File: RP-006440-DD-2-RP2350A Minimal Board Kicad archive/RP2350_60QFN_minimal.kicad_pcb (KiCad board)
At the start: 2 copper layers, 52 x 51 mm, 45 parts, among them J1 USB_C_Receptacle_USB2.0_16P, J2 Conn_02x18_Odd_Even, J3 Conn_02x18_Odd_Even, J4 SM03B-SRSS-TB, SW1 SW_Push, SW2 SW_Push, U1 RP2350_60QFN, U2 NCP1117-3.3_SOT223, U3 W25Q128JVS, Y1 ABM8-272-T3

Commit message: Schematic text
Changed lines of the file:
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@@
 		(tags "usb usb-c 2.0 pd")
 		(property "Reference" "J1"
-			(at 0 -5.645 360)
+			(at 0 -5.645 0)
 			(layer "F.SilkS")
 			(effects
@@
 		)
 		(property "Value" "USB_C_Receptacle_USB2.0_16P"
-			(at 0 5.1 360)
+			(at 0 5.1 0)
 			(layer "F.Fab")
 			(effects
@@
 		)
 		(fp_text user "${REFERENCE}"
-			(at 0 0 360)
+			(at 0 0 0)
 			(layer "F.Fab")
 			(effects
@@
 	)
 	(segment
-		(start 100 76)
-		(end 101.28 76)
+		(start 102.95 79.95)
+		(end 103.5 80.5)
 		(width 0.3)
 		(layer "F.Cu")
@@
 	)
 	(segment
-		(start 98.05 78.445)
-		(end 98.05 77.585305)
-		(width 0.3)
-		(layer "F.Cu")
-		(net 2)
-	)
-	(segment
-		(start 102.95 79.95)
-		(end 103.5 80.5)
-		(width 0.3)
-		(layer "F.Cu")
-		(net 2)
-	)
-	(segment
-		(start 99 77)
-		(end 100 76)
+		(start 99.72 76)
+		(end 101.28 76)
 		(width 0.3)
 		(layer "F.Cu")
@@
 	)
 	(segment
-		(start 98.635305 77)
-		(end 99 77)
+		(start 102.95 78.445)
+		(end 102.95 79.95)
 		(width 0.3)
 		(layer "F.Cu")
@@
 	)
 	(segment
-		(start 102.95 78.445)
-		(end 102.95 79.95)
+		(start 101.28 76)
+		(end 102.95 77.67)
 		(width 0.3)
 		(layer "F.Cu")
@@
 	)
 	(segment
-		(start 101.28 76)
-		(end 102.95 77.67)
+		(start 98.05 78.445)
+		(end 98.05 77.67)
 		(width 0.3)
 		(layer "F.Cu")
@@
 	)
 	(segment
-		(start 98.05 77.585305)
-		(end 98.635305 77)
+		(start 98.05 77.67)
+		(end 99.72 76)
 		(width 0.3)
 		(layer "F.Cu")

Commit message: small change
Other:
- board size 52 x 51 mm -> 52 x 65 mm
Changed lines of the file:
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@@
 	)
 	(gr_line
-		(start 123 121)
-		(end 77 121)
+		(start 123 135)
+		(end 77 135)
 		(stroke
 			(width 0.6)
@@
 	(gr_line
 		(start 126 73)
-		(end 126 118)
+		(end 126 132)
 		(stroke
 			(width 0.6)
@@
 	)
 	(gr_line
-		(start 74 118)
+		(start 74 132)
 		(end 74 73)
 		(stroke
@@
 	)
 	(gr_arc
-		(start 77 121)
-		(mid 74.87868 120.12132)
-		(end 74 118)
+		(start 77 135)
+		(mid 74.87868 134.12132)
+		(end 74 132)
 		(stroke
 			(width 0.6)
@@
 	)
 	(gr_arc
-		(start 126 118)
-		(mid 125.12132 120.12132)
-		(end 123 121)
+		(start 126 132)
+		(mid 125.12132 134.12132)
+		(end 123 135)
 		(stroke
 			(width 0.6)
@@
 		)
 	)
+	(dimension
+		(type aligned)
+		(layer "F.Cu")
+		(pts
+			(xy 74 132) (xy 126 132)
+		)
+		(height 15.999999)
+		(gr_text "52.0000 mm"
+			(at 100 146.199999 0)
+			(layer "F.Cu")
+			(effects
+				(font
+					(size 1.5 1.5)
+					(thickness 0.3)
+				)
+			)
+		)
+		(format
+			(prefix "")
+			(suffix "")
+			(units 3)
+			(units_format 1)
+			(precision 4)
+		)
+		(style
+			(thickness 0.2)
+			(arrow_length 1.27)
+			(text_position_mode 0)
+			(extension_height 0.58642)
+			(extension_offset 0.5) keep_text_aligned)
+	)
+	(dimension
+		(type aligned)
+		(layer "F.Cu")
+		(pts
+			(xy 77 135) (xy 77 70)
+		)
+		(height -13.5)
+		(gr_text "65.0000 mm"
+			(at 61.7 102.5 90)
+			(layer "F.Cu")
+			(effects
+				(font
+					(size 1.5 1.5)
+					(thickness 0.3)
+				)
+			)
+		)
+		(format
+			(prefix "")
+			(suffix "")
+			(units 3)
+			(units_format 1)
+			(precision 4)
+		)
+		(style
+			(thickness 0.2)
+			(arrow_length 1.27)
+			(text_position_mode 0)
+			(extension_height 0.58642)
+			(extension_offset 0.5) keep_text_aligned)
+	)
 	(segment
 		(start 97.9 91.4)
@@
 		(start 102.95 79.95)
 		(end 103.5 80.5)
-		(width 0.3)
+		(width 0.4)
 		(layer "F.Cu")
 		(net 2)
@@
 		(start 102.95 78.445)
 		(end 102.95 79.95)
-		(width 0.3)
+		(width 0.4)
 		(layer "F.Cu")
 		(net 2)
@@
 		(start 98.75 78.445)
 		(end 98.75 80.24)
-		(width 0.15)
+		(width 0.3)
 		(layer "F.Cu")
 		(net 59)

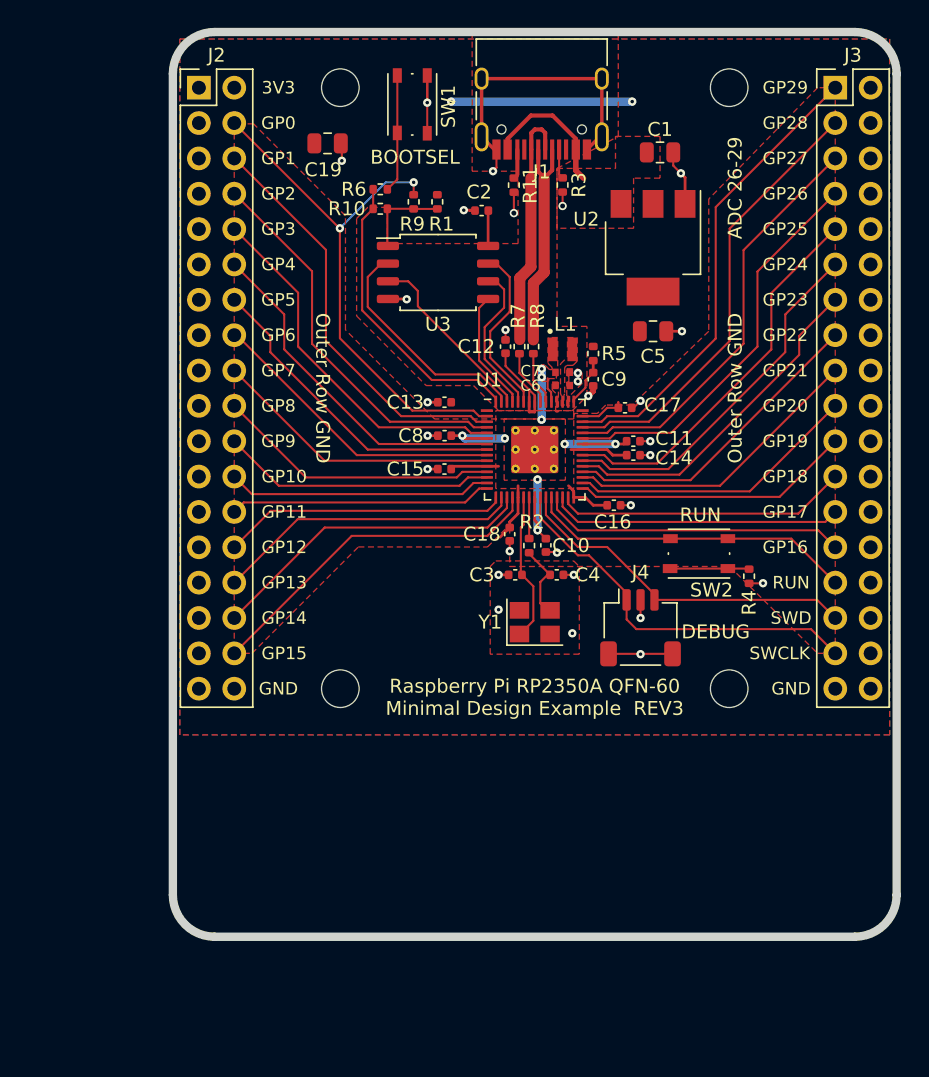
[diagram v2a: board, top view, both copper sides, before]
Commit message: Added footprints to PCB
debugger footprints pcb
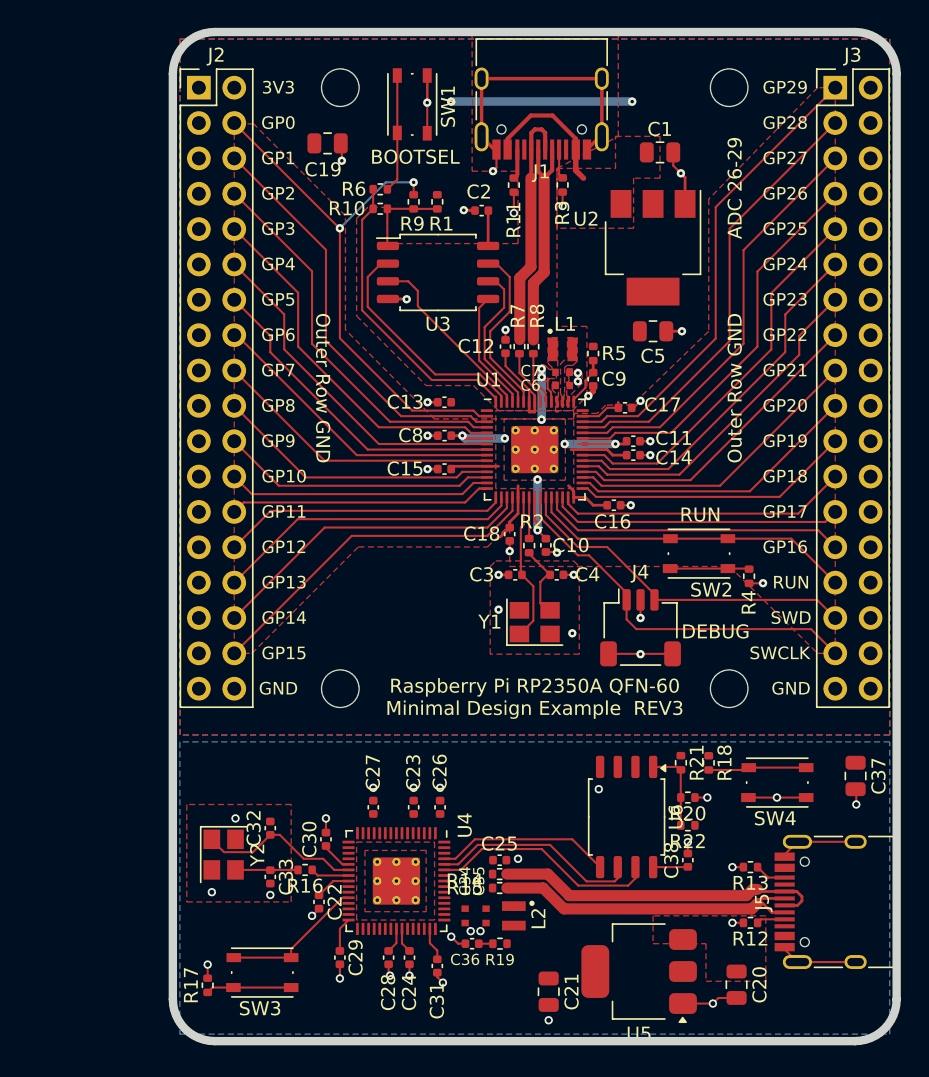
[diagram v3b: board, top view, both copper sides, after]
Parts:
- added C20: 10u, Capacitor_SMD:C_0805_2012Metric, F.Cu at (114.5, 138.4)
- added C21: 10u, Capacitor_SMD:C_0805_2012Metric, F.Cu at (101.0, 138.9)
- added C22: 100n, Capacitor_SMD:C_0402_1005Metric, F.Cu at (84.5, 132.5)
- added C23: 4.7u, Capacitor_SMD:C_0402_1005Metric, F.Cu at (91.3, 125.7)
- added C24: 100n, Capacitor_SMD:C_0402_1005Metric, F.Cu at (91.0, 136.5)
- added C25: 100n, Capacitor_SMD:C_0402_1005Metric, F.Cu at (97.5, 129.5)
- added C26: 100n, Capacitor_SMD:C_0402_1005Metric, F.Cu at (93.2, 125.7)
- added C27: 100n, Capacitor_SMD:C_0402_1005Metric, F.Cu at (88.4, 125.7)
- added C28: 100n, Capacitor_SMD:C_0402_1005Metric, F.Cu at (89.5, 136.5)
- added C29: 100n, Capacitor_SMD:C_0402_1005Metric, F.Cu at (86.0, 136.5)
- added C30: 100n, Capacitor_SMD:C_0402_1005Metric, F.Cu at (85.0, 128.0)
- added C31: 100n, Capacitor_SMD:C_0402_1005Metric, F.Cu at (93.0, 137.1)
- added C32: 15p, Capacitor_SMD:C_0402_1005Metric, F.Cu at (81.0, 127.2)
- added C33: 15p, Capacitor_SMD:C_0402_1005Metric, F.Cu at (81.0, 130.7)
- added C34: 4.7u, RP2350_60QFN_minimal:C_0402_1005Metric_small_pads, F.Cu at (95.0, 133.5)
- added C35: 4.7u, RP2350_60QFN_minimal:C_0402_1005Metric_small_pads, F.Cu at (96.5, 133.5)
- added C36: 4.7u, Capacitor_SMD:C_0402_1005Metric, F.Cu at (95.5, 135.5)
- added C37: 10u, Capacitor_SMD:C_0805_2012Metric, F.Cu at (123.0, 123.5)
- added C38: 100n, Capacitor_SMD:C_0402_1005Metric, F.Cu at (111.0, 129.5)
- added J5: USB_C_Receptacle_USB2.0_16P, Connector_USB:USB_C_Receptacle_HRO_TYPE-C-31-M-12, F.Cu at (122.0, 132.5)
- added L2: 3.3u, RP2350_60QFN_minimal:L_pol_2016, F.Cu at (98.5, 133.5)
- added R12: 5.1K, Resistor_SMD:R_0402_1005Metric, F.Cu at (115.5, 134.0)
- added R13: 5.1K, Resistor_SMD:R_0402_1005Metric, F.Cu at (115.5, 130.0)
- added R14: 27, Resistor_SMD:R_0402_1005Metric, F.Cu at (97.5, 130.5)
- added R15: 27, Resistor_SMD:R_0402_1005Metric, F.Cu at (97.5, 131.5)
- added R16: 1k, Resistor_SMD:R_0402_1005Metric, F.Cu at (83.5, 130.2)
- added R17: 1k, Resistor_SMD:R_0402_1005Metric, F.Cu at (76.5, 138.5)
- added R18: 1k, Resistor_SMD:R_0402_1005Metric, F.Cu at (112.5, 122.5)
- added R19: 33, Resistor_SMD:R_0402_1005Metric, F.Cu at (97.5, 135.5)
- added R20: DNF, Resistor_SMD:R_0402_1005Metric, F.Cu at (111.0, 125.0)
- added R21: 0, Resistor_SMD:R_0402_1005Metric, F.Cu at (110.5, 122.5)
- added R22: DNF, Resistor_SMD:R_0402_1005Metric, F.Cu at (111.0, 127.0)
- added SW3: SW_Push, Button_Switch_SMD:SW_Push_1P1T_NO_Vertical_Wuerth_434133025816, F.Cu at (80.4, 137.6)
- added SW4: SW_Push, Button_Switch_SMD:SW_Push_1P1T_NO_Vertical_Wuerth_434133025816, F.Cu at (117.4, 123.9)
- added TP1: TestPoint, TestPoint:TestPoint_Pad_1.5x1.5mm, B.Cu at (104.5, 137.5)
- added U4: RP2350_60QFN, RP2350_60QFN_minimal:RP2350-QFN-60-1EP_7x7_P0.4mm_EP3.4x3.4mm_ThermalVias, F.Cu at (90.1, 131.0)
- added U5: NCP1117-3.3_SOT223, Package_TO_SOT_SMD:SOT-223-3_TabPin2, F.Cu at (107.5, 137.5)
- added U6: W25Q128JVS, Package_SO:SOIC-8_5.23x5.23mm_P1.27mm, F.Cu at (106.6, 126.4)
- added Y2: ABM8-272-T3, Crystal:Crystal_SMD_3225-4Pin_3.2x2.5mm, F.Cu at (77.7, 129.1)
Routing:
- net GND: track 54.9 -> 85.4 mm, vias 29 -> 54
- net /debugprobe/USB_D+: track 0.00 -> 23.9 mm
- net /debugprobe/USB_D-: track 0.00 -> 23.1 mm
- net /debugprobe/QSPI_SD3: track 0.00 -> 16.5 mm
- net /debugprobe/QSPI_SCLK: track 0.00 -> 15.0 mm
- net /debugprobe/QSPI_SD0: track 0.00 -> 12.6 mm
- net /debugprobe/XIN: track 0.00 -> 11.8 mm
- net +3V3: track 41.4 -> 53.0 mm
- net /debugprobe/RUN: track 0.00 -> 10.4 mm
- net /debugprobe/~{USB_BOOT}: track 0.00 -> 7.07 mm
- net Net-(R17-Pad1): track 0.00 -> 6.14 mm
- net /debugprobe/FLASH_SS: track 0.00 -> 6.08 mm
- net Net-(C33-Pad1): track 0.00 -> 4.51 mm
- net +1V1: track 25.1 -> 29.4 mm
- net /debugprobe/XOUT: track 0.00 -> 2.78 mm
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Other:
- board size 52 x 65 mm -> 52 x 72.5 mm

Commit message: Updated PCB
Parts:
- moved L2 1.30 mm to (97.3, 133.0)
- moved C35 1.03 mm to (95.6, 133.0)
- moved C25 0.88 mm to (98.2, 129.0)
- moved C22 0.81 mm to (83.9, 131.9), turned to 180 degrees
- moved C23 0.76 mm to (91.0, 125.0)
- moved C34 0.61 mm to (94.7, 133.0)
- moved R19 0.54 mm to (97.0, 135.3)
- moved R14 0.50 mm to (97.5, 130.0)
- moved R15 0.50 mm to (97.5, 131.0)
- moved C27 0.45 mm to (88.8, 125.7)
- moved C36 0.45 mm to (95.1, 135.3)
- moved C24 0.31 mm to (91.2, 136.7)
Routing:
- net /debugprobe/QSPI_SD1: track 0.00 -> 17.7 mm
- net /debugprobe/QSPI_SD2: track 0.00 -> 15.6 mm
- net +1V1: track 29.4 -> 43.2 mm, vias 9 -> 18
- net +3V3: track 53.0 -> 63.2 mm
- net Net-(U4-USB_DP): track 0.00 -> 4.05 mm
- net Net-(U4-USB_DM): track 0.00 -> 3.80 mm
- net /debugprobe/VREG_AVDD: track 1.01 -> 3.61 mm
- net GND: track 85.4 -> 87.6 mm
- net /debugprobe/QSPI_SD0: track 12.6 -> 13.3 mm
- net /debugprobe/QSPI_SCLK: track 15.0 -> 15.8 mm
- net /debugprobe/QSPI_SD3: track 16.5 -> 17.1 mm
- added copper zone on F.Cu, net /debugprobe/VREG_LX

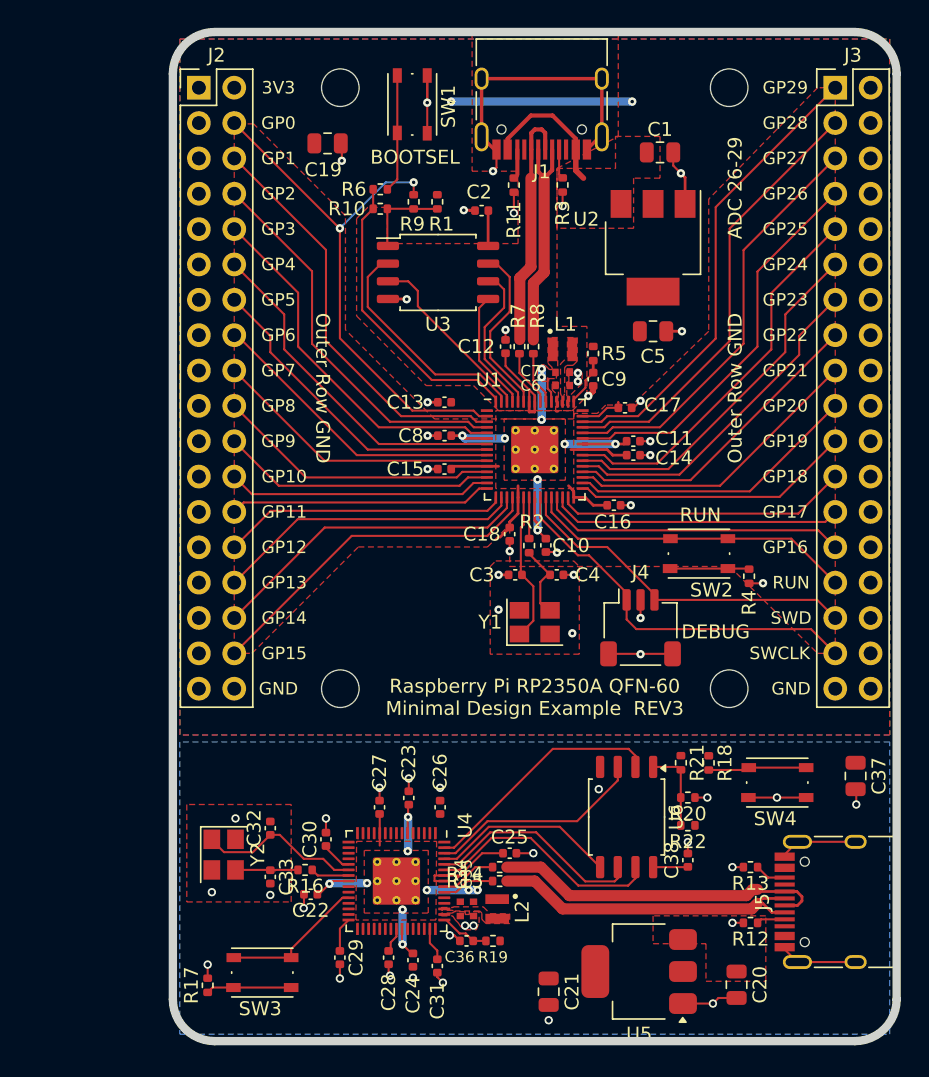
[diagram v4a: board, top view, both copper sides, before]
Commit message: Update schematic and PCB
Added hierarchal labels between main and debugprobe, connected the pins.
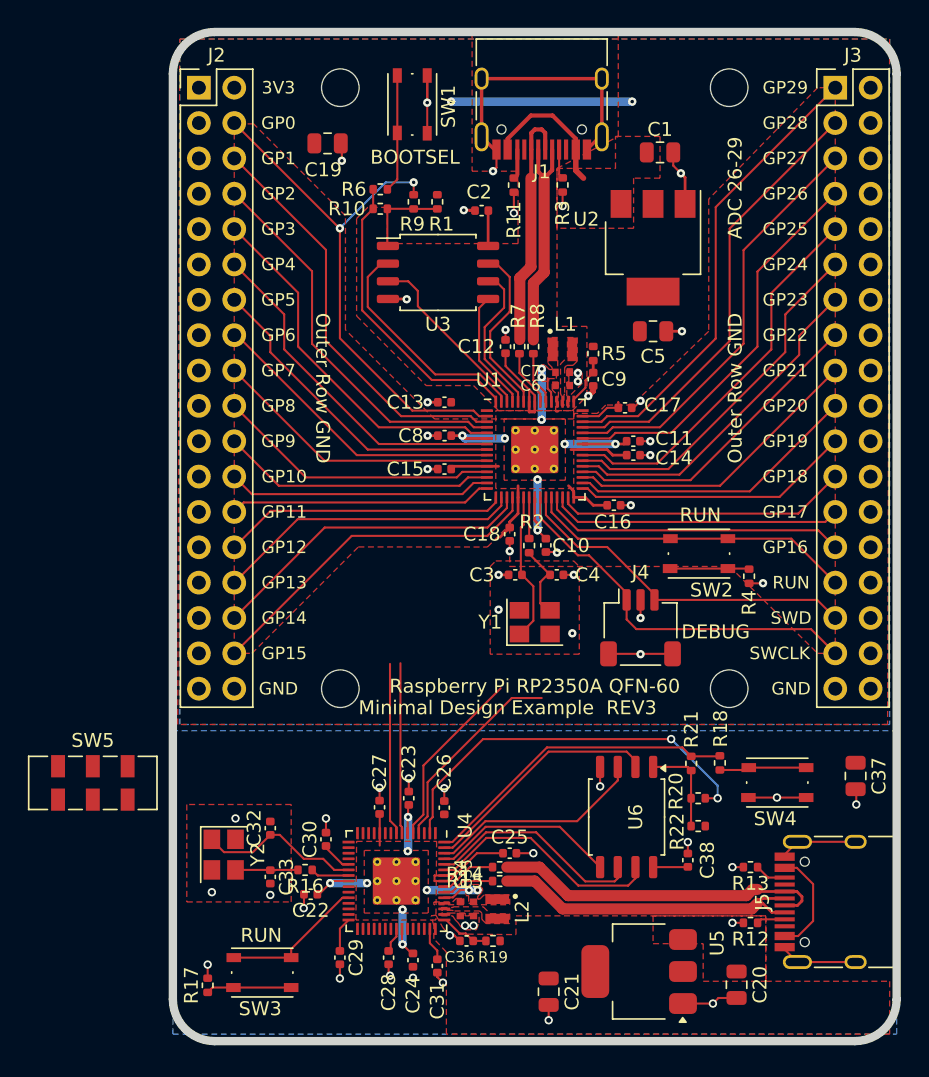
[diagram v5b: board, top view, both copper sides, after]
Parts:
- added SW5: SW_SPST, Button_Switch_SMD:SW_DPDT_CK_JS202011JCQN, F.Cu at (68.2, 124.0)
- moved R18 0.80 mm to (113.3, 122.5)
- moved R20 0.74 mm to (111.7, 125.0)
- moved R21 0.74 mm to (111.2, 122.5)
- moved R22 0.74 mm to (111.7, 127.0)
- moved C26 0.30 mm to (93.5, 125.7)
- renumbered TP1 to TP2
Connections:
- R18 pad 1: Net-(U4-QSPI_SS) -> /debugprobe/QSPI_SS
- U4 pad 2: unconnected-(U4-GPIO0-Pad2) -> /debugprobe/GPIO0
- U4 pad 24: /debugprobe/SWCLK -> /SWCLK
- U4 pad 25: /debugprobe/SWDIO -> /SWD
- U4 pad 4: /debugprobe/SWCLK -> /SWCLK
- U4 pad 5: /debugprobe/SWDIO -> /SWD
- U4 pad 60: Net-(U4-QSPI_SS) -> /debugprobe/QSPI_SS
- U4 pad 7: /debugprobe/UART1 -> /GPIO1
- U4 pad 8: /debugprobe/UART2 -> /GPIO0
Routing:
- net /debugprobe/GPIO0: track 0.89 -> 28.4 mm, vias 1 -> 2
- net /debugprobe/QSPI_SS: track 0.00 -> 22.9 mm
- net /SWCLK: track 27.8 -> 42.4 mm
- net /SWD: track 25.4 -> 38.4 mm
- net /GPIO0: track 39.0 -> 51.4 mm
- net /GPIO1: track 29.8 -> 42.1 mm
- net VBUS: track 10.1 -> 17.8 mm
- net GND: track 87.6 -> 91.0 mm
- net +1V1: track 43.2 -> 45.1 mm
- net /debugprobe/~{USB_BOOT}: track 7.07 -> 6.27 mm
- net /debugprobe/FLASH_SS: track 6.08 -> 6.82 mm

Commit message: Small change
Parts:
- renumbered TP2 to TP1
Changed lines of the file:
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@@
 		(descr "SMD rectangular pad as test Point, square 1.5mm side length")
 		(tags "test point SMD pad rectangle square")
-		(property "Reference" "TP2"
+		(property "Reference" "TP1"
 			(at 0 1.648 0)
 			(layer "B.SilkS")
